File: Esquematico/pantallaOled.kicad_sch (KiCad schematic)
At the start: 1 part

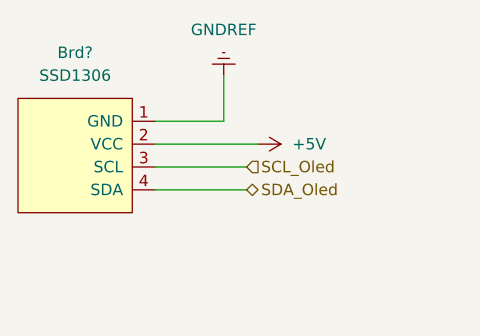
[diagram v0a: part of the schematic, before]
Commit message: actualizacion huellas resitencias y capacitorees
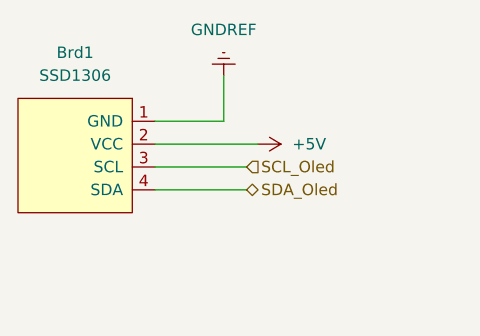
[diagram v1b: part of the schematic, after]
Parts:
- Brd1: renamed from Brd?; footprint SSD1306:128x64OLED -> Audio_Module:Reverb_BTDR-1H
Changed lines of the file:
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@@
   (symbol (lib_id "power:GNDREF") (at 160.02 83.82 180) (unit 1)
     (in_bom yes) (on_board yes) (fields_autoplaced)
-    (property "Reference" "#PWR?" (id 0) (at 160.02 77.47 0)
+    (property "Reference" "#PWR0138" (id 0) (at 160.02 77.47 0)
       (effects (font (size 1.27 1.27)) hide)
     )
@@
   (symbol (lib_id "SSD1306-128x64_OLED:SSD1306") (at 143.51 92.71 270) (unit 1)
     (in_bom yes) (on_board yes) (fields_autoplaced)
-    (property "Reference" "Brd?" (id 0) (at 143.51 81.28 90))
+    (property "Reference" "Brd1" (id 0) (at 143.51 81.28 90))
     (property "Value" "SSD1306" (id 1) (at 143.51 83.82 90))
-    (property "Footprint" "SSD1306:128x64OLED" (id 2) (at 149.86 92.71 0)
+    (property "Footprint" "Audio_Module:Reverb_BTDR-1H" (id 2) (at 149.86 92.71 0)
       (effects (font (size 1.27 1.27)) hide)
     )
@@
   (symbol (lib_id "power:+5V") (at 163.83 91.44 270) (unit 1)
     (in_bom yes) (on_board yes) (fields_autoplaced)
-    (property "Reference" "#PWR?" (id 0) (at 160.02 91.44 0)
+    (property "Reference" "#PWR0139" (id 0) (at 160.02 91.44 0)
       (effects (font (size 1.27 1.27)) hide)
     )

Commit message: Huellas asignadas. Revisar si algunos de los módulos serán cambiados por conectores Molex.
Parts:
- Brd1: footprint Audio_Module:Reverb_BTDR-1H -> SSD1306:128x64OLED
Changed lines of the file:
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@@
     (property "Reference" "Brd1" (id 0) (at 143.51 81.28 90))
     (property "Value" "SSD1306" (id 1) (at 143.51 83.82 90))
-    (property "Footprint" "Audio_Module:Reverb_BTDR-1H" (id 2) (at 149.86 92.71 0)
+    (property "Footprint" "SSD1306:128x64OLED" (id 2) (at 149.86 92.71 0)
       (effects (font (size 1.27 1.27)) hide)
     )
